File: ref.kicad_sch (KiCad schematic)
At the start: 20 parts, among them Q1 Q_NPN_BCE, U4 ADR1000, U5 Opamp_Dual

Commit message: asdf
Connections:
- net 0Vin: now also C13.1, U5.4 (V-)
- net 12Vin: now also C13.2, U5.8 (V+)
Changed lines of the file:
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@@
   (junction (at 132.08 110.49) (diameter 0) (color 0 0 0 0)
   )
-  (junction (at 30.48 41.91) (diameter 0) (color 0 0 0 0)
-  )
   (junction (at 132.08 96.52) (diameter 0) (color 0 0 0 0)
   )
@@
   (junction (at 128.27 57.15) (diameter 0) (color 0 0 0 0)
   )
-  (junction (at 30.48 95.25) (diameter 0) (color 0 0 0 0)
-  )
   (junction (at 132.08 109.22) (diameter 0) (color 0 0 0 0)
   )
@@
     (stroke (width 0) (type default) (color 0 0 0 0))
   )
-  (wire (pts (xy 49.53 95.25) (xy 30.48 95.25))
-    (stroke (width 0) (type default) (color 0 0 0 0))
-  )
   (wire (pts (xy 123.19 44.45) (xy 128.27 44.45))
     (stroke (width 0) (type default) (color 0 0 0 0))
@@
     (stroke (width 0) (type default) (color 0 0 0 0))
   )
-  (wire (pts (xy 27.94 95.25) (xy 30.48 95.25))
+  (wire (pts (xy 27.94 95.25) (xy 49.53 95.25))
     (stroke (width 0) (type default) (color 0 0 0 0))
   )
@@
     (stroke (width 0) (type default) (color 0 0 0 0))
   )
-  (wire (pts (xy 30.48 41.91) (xy 49.53 41.91))
+  (wire (pts (xy 27.94 41.91) (xy 49.53 41.91))
     (stroke (width 0) (type default) (color 0 0 0 0))
   )
@@
     (stroke (width 0) (type default) (color 0 0 0 0))
   )
-  (wire (pts (xy 30.48 36.83) (xy 30.48 41.91))
-    (stroke (width 0) (type default) (color 0 0 0 0))
-  )
   (wire (pts (xy 73.66 125.73) (xy 81.28 125.73))
     (stroke (width 0) (type default) (color 0 0 0 0))
@@
     (stroke (width 0) (type default) (color 0 0 0 0))
   )
-  (wire (pts (xy 30.48 95.25) (xy 30.48 100.33))
-    (stroke (width 0) (type default) (color 0 0 0 0))
-  )
   (wire (pts (xy 105.41 96.52) (xy 107.95 96.52))
     (stroke (width 0) (type default) (color 0 0 0 0))
@@
     (stroke (width 0) (type default) (color 0 0 0 0))
   )
-  (wire (pts (xy 27.94 41.91) (xy 30.48 41.91))
-    (stroke (width 0) (type default) (color 0 0 0 0))
-  )
   (wire (pts (xy 93.98 46.99) (xy 93.98 57.15))
     (stroke (width 0) (type default) (color 0 0 0 0))
@@
   (wire (pts (xy 148.59 57.15) (xy 161.29 57.15))
     (stroke (width 0) (type default) (color 0 0 0 0))
-  )
-  (label "GNDf" (at 30.48 100.33 0)
-    (effects (font (size 1.27 1.27)) (justify left bottom))
   )
   (label "ADR_Pin6" (at 114.3 71.12 180)
@@
     (effects (font (size 0.5 0.5)) (justify right bottom))
   )
-  (label "12Vf" (at 30.48 36.83 0)
-    (effects (font (size 1.27 1.27)) (justify left bottom))
-  )
   (label "ADR_Pin3" (at 132.08 59.69 0)
     (effects (font (size 0.5 0.5)) (justify left bottom))
@@
     (effects (font (size 1.27 1.27)) (justify left))
   )
+  (hierarchical_label "12Vin" (shape input) (at 73.66 107.95 180)
+    (effects (font (size 1.27 1.27)) (justify right))
+  )
   (hierarchical_label "guard" (shape output) (at 217.17 100.33 0)
     (effects (font (size 1.27 1.27)) (justify left))
@@
     (effects (font (size 1.27 1.27)) (justify left))
   )
+  (hierarchical_label "0Vin" (shape input) (at 73.66 125.73 180)
+    (effects (font (size 1.27 1.27)) (justify right))
+  )
   (symbol (lib_id "Device:D") (at 156.21 44.45 0) (unit 1)

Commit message: started proto area
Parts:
- added R23, R25, R27, R29, R31: dnp, Resistor_SMD:R_0805_2012Metric, symbol Device:R
- added R24, R26, R28, R30, R32: dnp, Crystal:Crystal_HC52-U_Vertical, symbol Device:R
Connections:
- net ADR: now also R23.2, R24.2, R29.2, R30.2; no longer RN1.5 (R5.1), U4.3 (VREF)
- net ADR_Pin5: now also R27.1, R28.1; no longer RN1.14 (R1.2)
- net ADR_Pin8: now also R25.1, R26.1; no longer RN1.13 (R2.2)
- net at R13.1, R14.1: now also RN1.6 (R6.1)
- net at RN1.7 (R7.1): now also R31.2, R32.2
- new net: R25.2, R26.2, RN1.13 (R2.2)
- new net: R23.1, R24.1, RN1.5 (R5.1)
- new net: R31.1, R32.1
- new net: R27.2, R28.2, RN1.14 (R1.2)
- new net ADR_Pin3: R29.1, R30.1, U4.3 (VREF)
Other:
- moved on the sheet: C13, D4, RN1A, RN1B, RN1F, RN1G, U5C

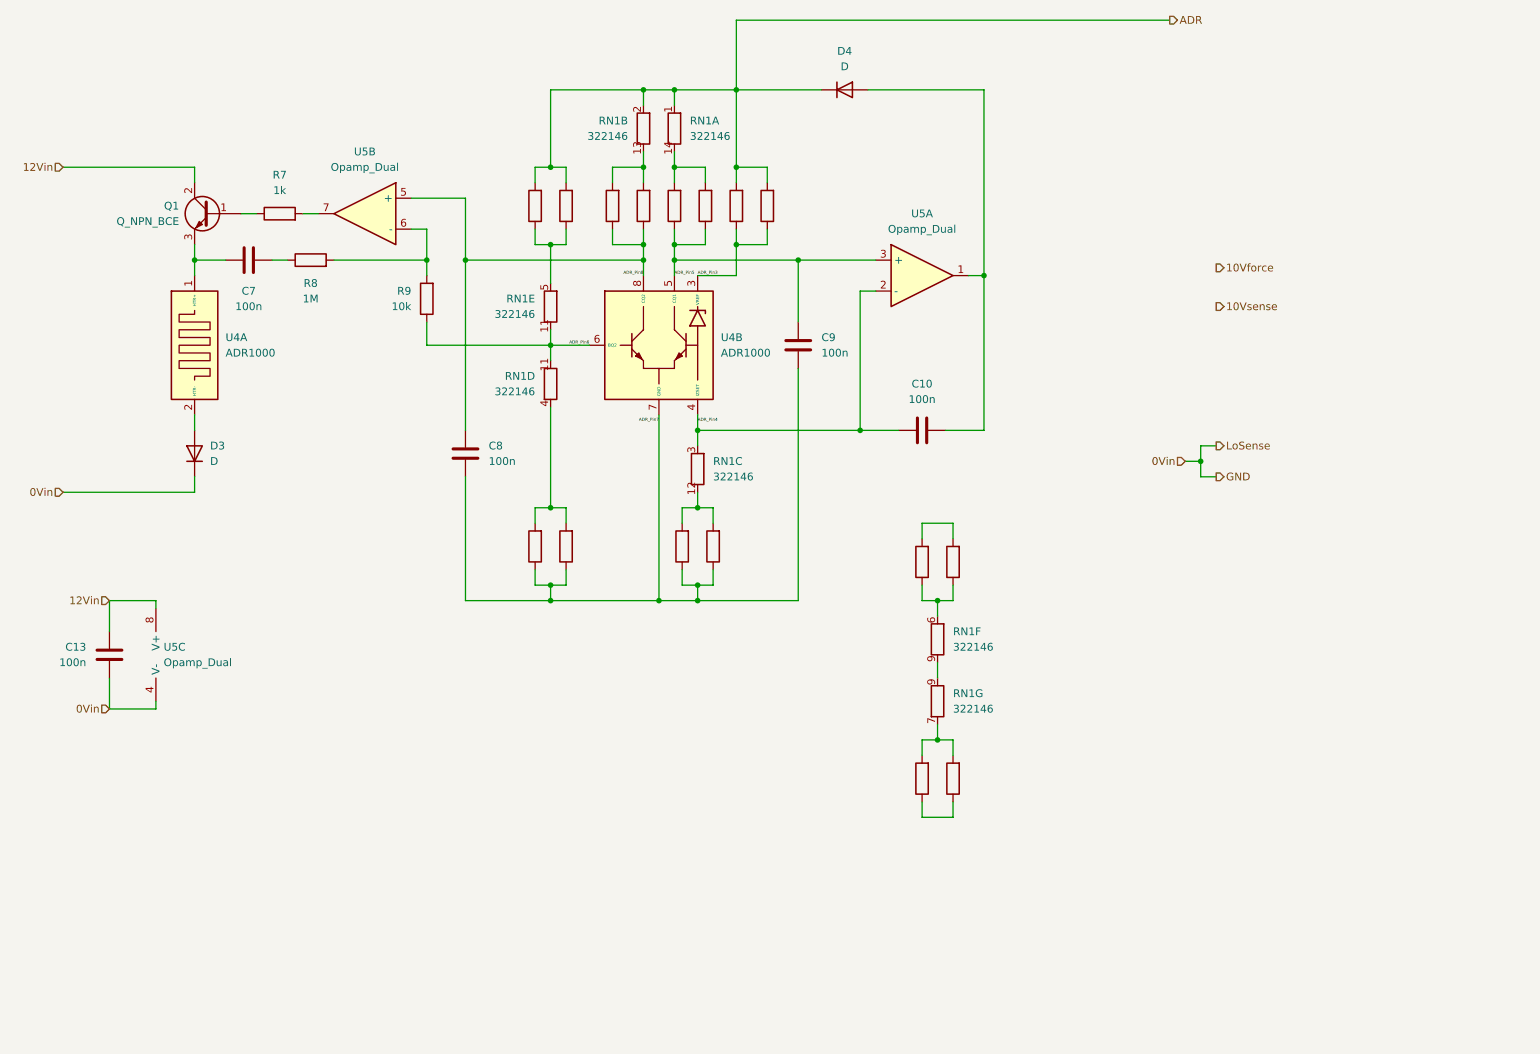
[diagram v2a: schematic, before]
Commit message: added 10V buffer
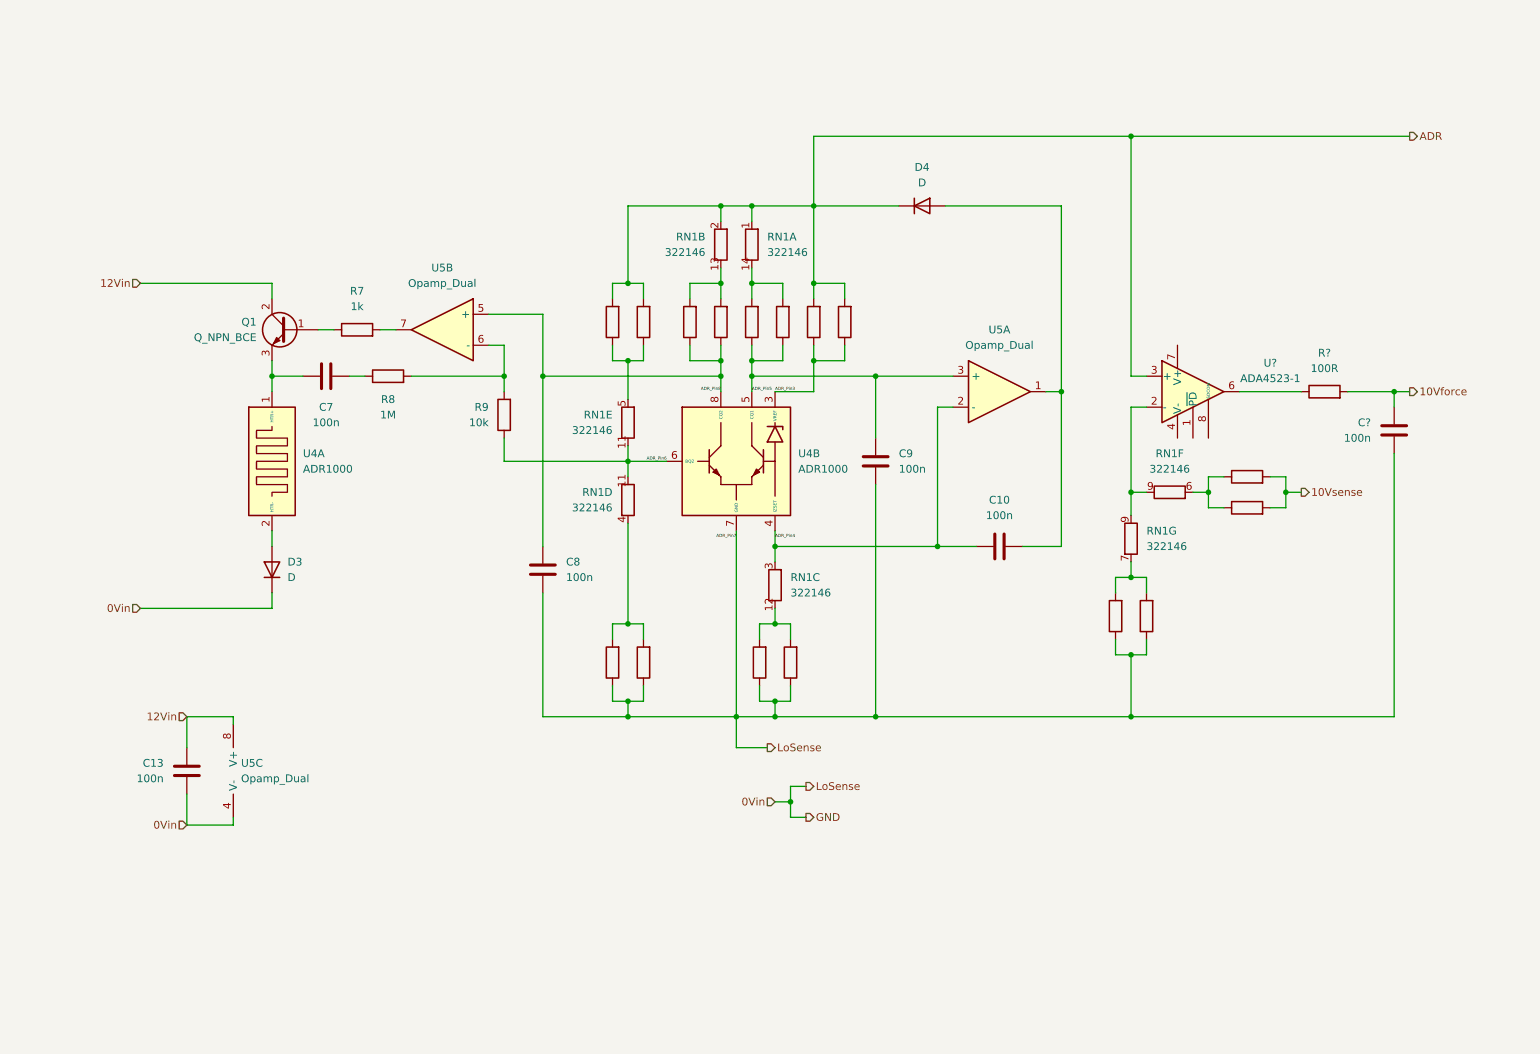
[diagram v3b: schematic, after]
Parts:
- added C?: 100n, Capacitor_SMD:C_0805_2012Metric, symbol Device:C
- added R?: 100R, Resistor_SMD:R_0805_2012Metric, symbol Device:R
- added U?: ADA4523-1, Package_SO:SOIC-8_3.9x4.9mm_P1.27mm, symbol ADRmu_Library:ADA4523-1
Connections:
- net ADR_Pin7 is gone; now on net 0Vin: C8.1, C9.1, R15.1, R16.1, R17.1, R18.1, U4.7 (GND)
- net 0Vin: now also R31.1, R32.1, C?.1
- net 10Vforce: now also C?.2, R?.2
- net 10Vsense: now also R13.2, R14.2
- net ADR: now also U?.3 (+)
- net at RN1.9 (R6.2), RN1.9 (R7.2): now also U?.2 (-)
- new net: R?.1, U?.6
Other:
- moved on the sheet: C10, C13, C7, C8, C9, D3, D4, Q1, R7, R8, R9, RN1A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

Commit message: the small reset
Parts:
- removed R13, R23, R25, R27, R29, R31: dnp, Resistor_SMD:R_0805_2012Metric, symbol Device:R
- removed R14, R24, R26, R28, R30, R32: dnp, Crystal:Crystal_HC52-U_Vertical, symbol Device:R
- removed R15, R17: 0, Resistor_SMD:R_0805_2012Metric, symbol Device:R
- removed R16, R18: 0, Crystal:Crystal_HC52-U_Vertical, symbol Device:R
- added C19: 100n, Capacitor_SMD:C_0805_2012Metric, symbol Device:C
- added NT2: NetTie_2, NetTie:NetTie-2_SMD_Pad0.5mm, symbol Device:NetTie_2
- gave numbers to parts that had none: 3
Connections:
- net 12Vin is gone; now on net DC_DC_Vin+: C13.2, Q1.2 (C), U5.8 (V+)
- net ADR_Pin3 is gone; now on net ADR: U4.3 (VREF)
- net 10Vsense: now also RN1.6 (R6.1)
- net ADR: now also RN1.5 (R5.1)
- net ADR_Pin5: now also RN1.14 (R1.2)
- net ADR_Pin8: now also RN1.13 (R2.2)
- net LoSense: now reaches RN1.12 (R3.2)
- net LoSense: now also C18.1, C8.1, C9.1, RN1.4 (R4.1), RN1.7 (R7.1), U4.7 (GND), NT2.2
- net DC_DC_GND: now reaches U8.4 (V-)
- net DC_DC_GND: now also C13.1, D3.1 (K), U5.4 (V-), C19.1, NT2.1
- net DC_DC_Vin+: now reaches U8.7 (V+)
- net DC_DC_Vin+: now also C19.2
- removed net 0Vin: C13.1, C18.1, C8.1, C9.1, D3.1 (K), U4.7 (GND), U5.4 (V-)
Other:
- moved on the sheet: C18, D4, R33, RN1A, RN1B, RN1F, RN1G, U8

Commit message: asdf?
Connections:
- net DC_DC_GND: now also C8.1, C9.1
- net LoSense: no longer C8.1, C9.1
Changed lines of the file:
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@@
   (junction (at 144.78 116.84) (diameter 0) (color 0 0 0 0)
   )
+  (junction (at 106.68 120.65) (diameter 0) (color 0 0 0 0)
+  )
   (junction (at 48.26 132.08) (diameter 0) (color 0 0 0 0)
   )
@@
   (junction (at 200.66 102.87) (diameter 0) (color 0 0 0 0)
   )
-  (junction (at 161.29 116.84) (diameter 0) (color 0 0 0 0)
-  )
   (junction (at 191.77 78.74) (diameter 0) (color 0 0 0 0)
   )
@@
   (junction (at 135.89 63.5) (diameter 0) (color 0 0 0 0)
   )
-  (junction (at 106.68 116.84) (diameter 0) (color 0 0 0 0)
-  )
   (junction (at 100.33 76.2) (diameter 0) (color 0 0 0 0)
   )
@@
     (stroke (width 0) (type default) (color 0 0 0 0))
   )
+  (wire (pts (xy 161.29 93.98) (xy 161.29 120.65))
+    (stroke (width 0) (type default) (color 0 0 0 0))
+  )
   (wire (pts (xy 62.23 111.76) (xy 62.23 116.84))
     (stroke (width 0) (type default) (color 0 0 0 0))
@@
     (stroke (width 0) (type default) (color 0 0 0 0))
   )
-  (wire (pts (xy 161.29 116.84) (xy 200.66 116.84))
+  (wire (pts (xy 144.78 116.84) (xy 200.66 116.84))
     (stroke (width 0) (type default) (color 0 0 0 0))
   )
@@
     (stroke (width 0) (type default) (color 0 0 0 0))
   )
-  (wire (pts (xy 106.68 116.84) (xy 120.65 116.84))
-    (stroke (width 0) (type default) (color 0 0 0 0))
-  )
   (wire (pts (xy 135.89 73.66) (xy 135.89 76.2))
     (stroke (width 0) (type default) (color 0 0 0 0))
@@
     (stroke (width 0) (type default) (color 0 0 0 0))
   )
+  (wire (pts (xy 62.23 116.84) (xy 62.23 120.65))
+    (stroke (width 0) (type default) (color 0 0 0 0))
+  )
   (wire (pts (xy 135.89 76.2) (xy 135.89 78.74))
     (stroke (width 0) (type default) (color 0 0 0 0))
@@
     (stroke (width 0) (type default) (color 0 0 0 0))
   )
-  (wire (pts (xy 86.36 116.84) (xy 106.68 116.84))
+  (wire (pts (xy 86.36 116.84) (xy 120.65 116.84))
     (stroke (width 0) (type default) (color 0 0 0 0))
   )
@@
     (stroke (width 0) (type default) (color 0 0 0 0))
   )
+  (wire (pts (xy 106.68 120.65) (xy 161.29 120.65))
+    (stroke (width 0) (type default) (color 0 0 0 0))
+  )
   (wire (pts (xy 40.64 60.96) (xy 62.23 60.96))
     (stroke (width 0) (type default) (color 0 0 0 0))
@@
     (stroke (width 0) (type default) (color 0 0 0 0))
   )
-  (wire (pts (xy 106.68 111.76) (xy 106.68 116.84))
-    (stroke (width 0) (type default) (color 0 0 0 0))
-  )
   (wire (pts (xy 44.45 149.86) (xy 48.26 149.86))
     (stroke (width 0) (type default) (color 0 0 0 0))
@@
     (stroke (width 0) (type default) (color 0 0 0 0))
   )
-  (wire (pts (xy 144.78 116.84) (xy 161.29 116.84))
-    (stroke (width 0) (type default) (color 0 0 0 0))
-  )
   (wire (pts (xy 140.97 63.5) (xy 144.78 63.5))
     (stroke (width 0) (type default) (color 0 0 0 0))
@@
     (stroke (width 0) (type default) (color 0 0 0 0))
   )
+  (wire (pts (xy 62.23 120.65) (xy 106.68 120.65))
+    (stroke (width 0) (type default) (color 0 0 0 0))
+  )
   (wire (pts (xy 200.66 76.2) (xy 212.09 76.2))
     (stroke (width 0) (type default) (color 0 0 0 0))
@@
     (stroke (width 0) (type default) (color 0 0 0 0))
   )
+  (wire (pts (xy 106.68 111.76) (xy 106.68 120.65))
+    (stroke (width 0) (type default) (color 0 0 0 0))
+  )
   (wire (pts (xy 62.23 101.6) (xy 62.23 104.14))
     (stroke (width 0) (type default) (color 0 0 0 0))
@@
     (stroke (width 0) (type default) (color 0 0 0 0))
   )
-  (wire (pts (xy 161.29 93.98) (xy 161.29 116.84))
-    (stroke (width 0) (type default) (color 0 0 0 0))
-  )

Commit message: send halp
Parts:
- added JP10, JP11, JP5, JP6, JP7, JP8, JP9, JP?: Jumper_2_Bridged, Jumper:SolderJumper-2_P1.3mm_Bridged_RoundedPad1.0x1.5mm, symbol Jumper:Jumper_2_Bridged
- added R13, R15, R17, R24, R25, R27, R29, R?: 0, Resistor_SMD:R_0805_2012Metric, symbol Device:R
- added R14, R16, R18, R23, R26, R28, R30, R?: 0, Crystal:Crystal_HC52-U_Vertical, symbol Device:R
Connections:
- net 10Vsense: now also JP9.2 (B), R25.2, R26.2; no longer RN1.6 (R6.1)
- net ADR: now also JP10.2 (B), JP11.2 (B), JP?.2 (B), R27.2, R28.2, R29.2, R30.2, R?.2, R?.2; no longer RN1.1 (R2.1), RN1.2 (R2.1), RN1.5 (R5.1)
- net LoSense: now also JP6.2 (B), JP7.2 (B), JP8.2 (B), R13.2, R14.2, R17.2, R18.2, R23.2, R24.2; no longer RN1.12 (R3.2), RN1.4 (R4.1), RN1.7 (R7.1)
- new net: JP6.1 (A), R13.1, R14.1, RN1.12 (R3.2)
- new net: JP7.1 (A), R17.1, R18.1, RN1.4 (R4.1)
- new net: JP9.1 (A), R25.1, R26.1, RN1.6 (R6.1)
- new net: JP?.1 (A), R?.1, R?.1, RN1.5 (R5.1)
- new net: JP8.1 (A), R23.1, R24.1, RN1.7 (R7.1)
- new net: JP5.1 (A), R15.1, R16.1
- new net: JP5.2 (B), R15.2, R16.2
- new net: JP10.1 (A), R27.1, R28.1, RN1.1 (R2.1)
- new net: JP11.1 (A), R29.1, R30.1, RN1.2 (R2.1)
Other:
- moved on the sheet: C13, C19, D4, NT2, RN1G, U5C

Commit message: net classes
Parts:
- added JP13: Jumper_2_Open, Jumper:SolderJumper-2_P1.3mm_Open_RoundedPad1.0x1.5mm, symbol Jumper:Jumper_2_Open
- gave numbers to parts that had none: 3
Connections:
- net ADR: now also JP5.2 (B), R15.2, R16.2; no longer U4.3 (VREF)
- net ADR_Pin6: now also JP13.1 (A)
- net U5_Pin1: now reaches C10.1, D4.2 (A), U5.1
- net RN1_Pin12: now reaches JP6.1 (A), R13.1, R14.1, RN1.12 (R3.2)
- net RN1_Pin4: now reaches JP7.1 (A), R17.1, R18.1, RN1.4 (R4.1)
- net RN1_Pin4: now also JP13.2 (B)
- net RN1_Pin6: now reaches JP9.1 (A), R25.1, R26.1, RN1.6 (R6.1)
- net ADR_Pin1: now reaches C7.1, Q1.3 (E), U4.1 (HTR+)
- net ADR_Pin2: now reaches D3.2 (A), U4.2 (HTR-)
- net RN1_Pin5: now reaches JP12.1 (A), R31.1, R32.1, RN1.5 (R5.1)
- net RN1_Pin7: now reaches JP8.1 (A), R23.1, R24.1, RN1.7 (R7.1)
- net RN1_Pin7: now also JP10.1 (A), R27.1, R28.1, RN1.1 (R2.1)
- net ADR_Pin3: now reaches JP5.1 (A), R15.1, R16.1
- net ADR_Pin3: now also U4.3 (VREF)
- net U8_Pin2: now reaches RN1.9 (R6.2), RN1.9 (R7.2), U8.2 (-)
- net U8_Pin6: now reaches R33.1, U8.6
- net Q1_Pin1: now reaches Q1.1 (B), R7.1
- net U5_Pin7: now reaches R7.2, U5.7
- net RN1_Pin2: now reaches JP11.1 (A), R29.1, R30.1, RN1.2 (R2.1)
- net U5_Pin6: now reaches R8.2, R9.2, U5.6 (-)
- net R8_Pin1: now reaches C7.2, R8.1
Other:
- moved on the sheet: JP5, R15, R16, RN1D

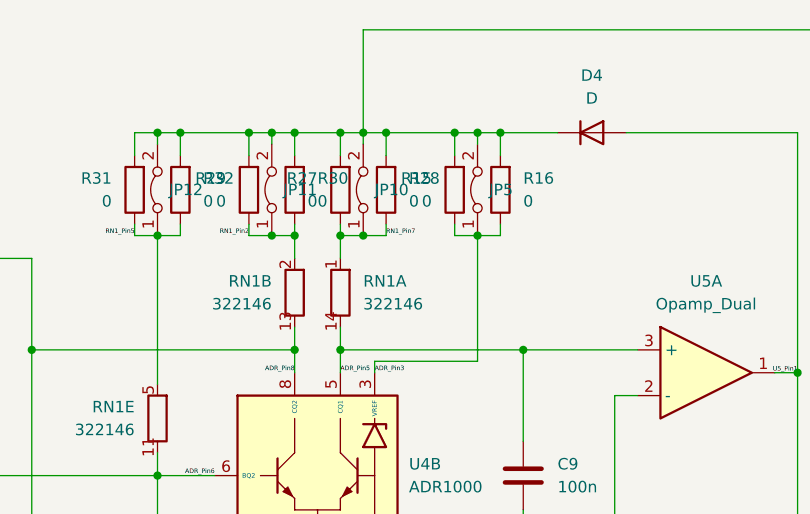
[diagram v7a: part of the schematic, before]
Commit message: trace widths based on net classes
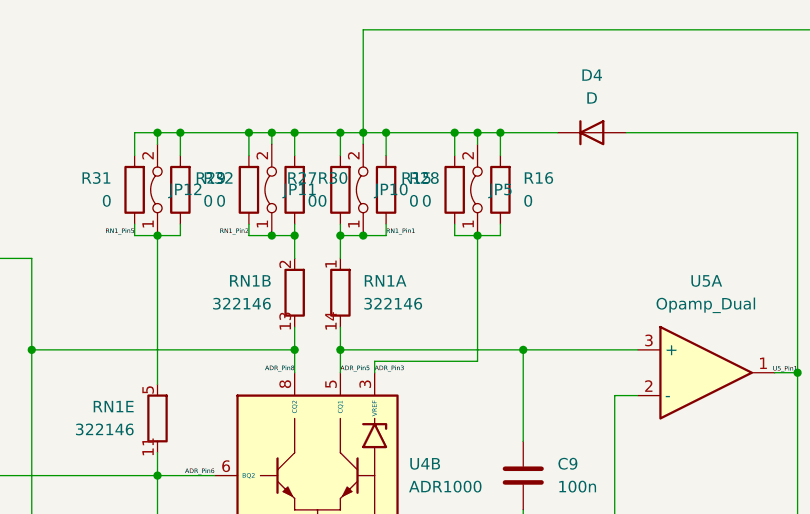
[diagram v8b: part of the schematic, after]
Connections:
- net RN1_Pin7: no longer JP10.1 (A), R27.1, R28.1, RN1.1 (R2.1)
- new net RN1_Pin1: JP10.1 (A), R27.1, R28.1, RN1.1 (R2.1)
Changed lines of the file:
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@@
     (effects (font (size 0.5 0.5)) (justify right bottom))
   )
-  (label "RN1_Pin7" (at 146.05 63.5 0)
+  (label "RN1_Pin1" (at 146.05 63.5 0)
     (effects (font (size 0.5 0.5)) (justify left bottom))
   )
